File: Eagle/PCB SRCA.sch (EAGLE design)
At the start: 65 parts, among them IC1 DSPIC30F4011-30I_P, IC2 LM324LVIDR, IC3 LMT86QDCKRQ1, IC4 LORA_MOTE, J1 TBL002A-350-03GR-2OR, J2 TBL002A-350-03GR-2OR, J3 TBL002A-350-03GR-2OR, J4 172447-0004, J5 ICSP, Q1 TIP41C, T1 2N3904, T10 2N3904, T11 2N3904, T12 2N3904, T13 2N3904, T2 2N3904, T3 2N3904, T4 2N3904, T5 2N3904, T6 2N3904, T7 2N3904, T8 2N3904, T9 2N3904

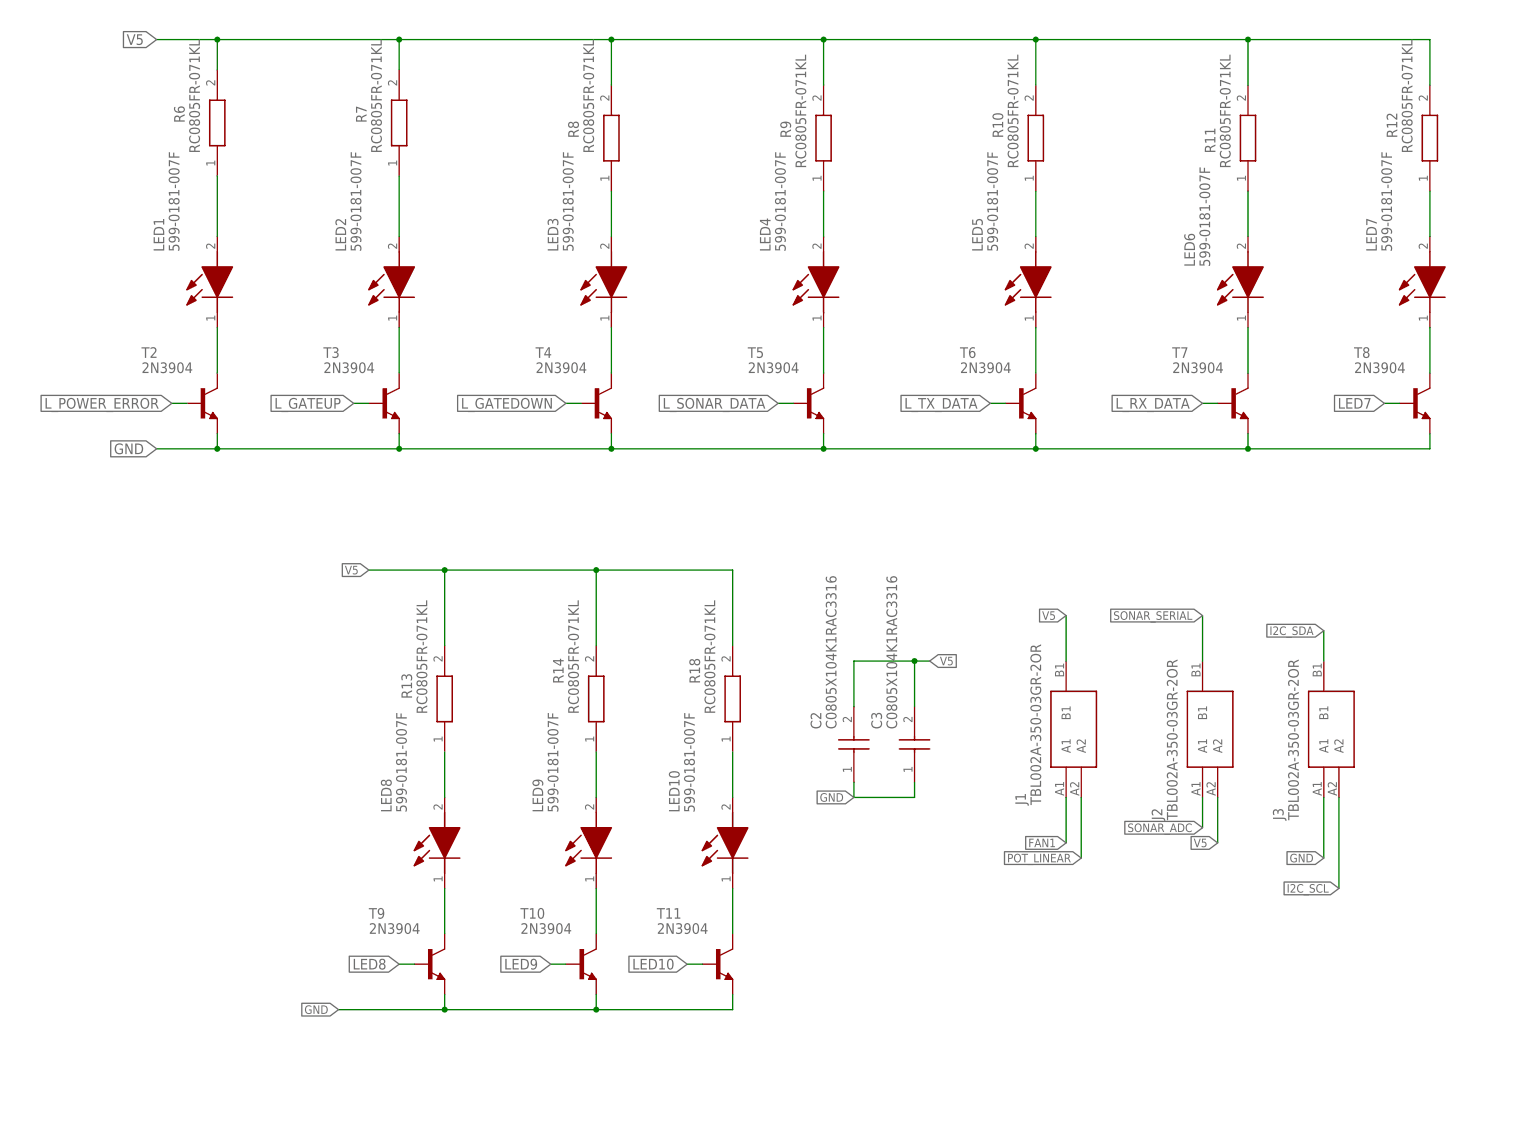
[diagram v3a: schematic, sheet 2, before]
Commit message: 11/08/2021
cambios pre finales del pcb y sus componentes
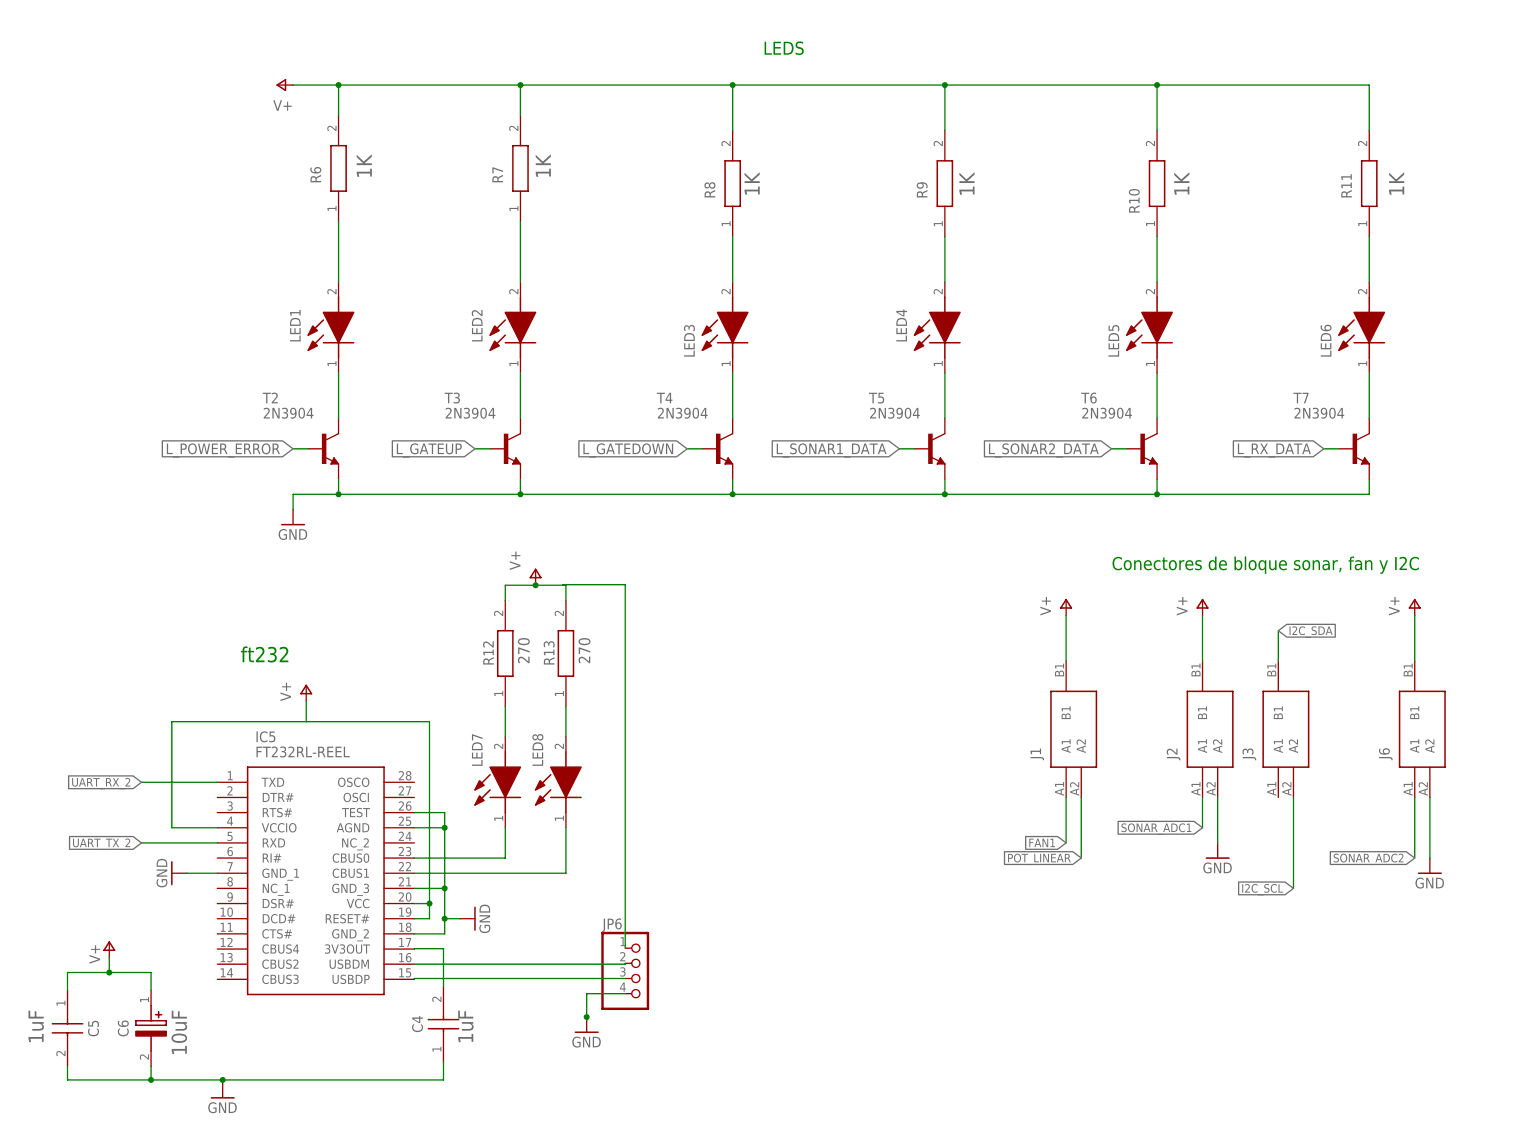
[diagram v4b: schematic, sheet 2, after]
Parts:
- removed LED10, LED9: 599-0181-007F, 599-0181-007F:599-0181-007F
- removed R14, R18: RC0805FR-071KL, RC0805FR-071KL:RC0805FR-071KL
- removed T10, T11, T8, T9: 2N3904, transistor-neu-to92:2N3904
- added C4, C5: C0805X104K1RAC3316, C0805X104K1RAC3316:C0805X104K1RAC3316
- added C6: UUP1C100MCL1GS, UUP1C100MCL1GS:UUP1C100MCL1GS
- added IC5: FT232RL-REEL, FT232RL-REEL:FT232RL-REEL
- added J6: TBL002A-350-03GR-2OR, TBL002A-350-03GR-2OR:TBL002A-350-03GR-2OR
- added J7: 44914-0401, 44914-0401:44914-0401
- added JP1, JP2, JP3, JP4: (no value), jumper:JP1E
- added JP5: (no value), pinhead:PINHD-1X6
- added JP6: (no value), pinhead:PINHD-1X4
- added ON: 599-0181-007F, 599-0181-007F:599-0181-007F
- added R24: RC0805FR-071KL, RC0805FR-071KL:RC0805FR-071KL
- added R25, R26: (no value), rcl:R-EU_0204/7
- added R27, R28: (no value), rcl:R-EU_0207/10
- C2, C3: value C0805X104K1RAC3316 -> TAJR104K020RNJ; device C0805X104K1RAC3316:C0805X104K1RAC3316 -> TAJR104K020RNJ:TAJR104K020RNJ
- J4: value 172447-0004 -> 44914-0801; device 172447-0004:172447-0004 -> 44914-0801:44914-0801
- R1: value RC0805FR-071KL -> (none); device RC0805FR-071KL:RC0805FR-071KL -> rcl:R-EU_0204/7
- renumbered LS1 to ICS
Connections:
- net N$3 renamed TEMP3
- net SONAR_ADC renamed SONAR_ADC1
- removed net LED10: IC1.OC4/RD3, T11.B
- removed net LED7: IC1.OSC2/CLKO/RC15, T8.B
- removed net LED8: IC1.!FLTA!/INT0/RE8, T9.B
- removed net LED9: IC1.EMUD2/OC2/IC2/INT2/RD1, T10.B
- removed net L_SONAR_DATA: IC1.AN6/OCFA/RB6, T5.B
- removed net L_TX_DATA: IC1.AN7/RB7, T6.B
- removed net N$13 (its old number): LED7.K, T8.C
- removed net SONAR_SERIAL: IC1.U2RX/CN17/RF4, J2.B1
- removed net TX_UART2: IC1.U2TX/CN18/RF5
- removed net V5: C2.2, C3.2, D1.C, IC1.VDD_1, IC1.VDD_3, IC2.V+, IC3.VDD_1, IC4.V5, ICS.1, J1.B1, J2.A2, J4.4, J5.VDD, R1.2, R10.2, R11.2, R12.2, R13.2, R14.2, R17.2, R18.2, R19.2, R2.2, R6.2, R7.2, R8.2, R9.2, S2.NO_1, S3.NO_2, S4.NO_1
- new net BIT_1: IC1.PWM2L/RE2, J4.1
- new net BIT_2: IC1.PWM2H/RE3, J4.2
- new net BIT_3: IC1.PWM3L/RE4, J4.3
- new net BIT_4: IC1.PWM3H/RE5, J4.4
- new net BIT_5: IC1.C1RX/RF0, J4.5
- new net BIT_6: IC1.C1TX/RF1, J4.6
- new net BIT_7: IC1.SCK1/RF6, J4.7
- new net BIT_8: IC1.EMUC2/OC1/IC1/INT1/RD0, J4.8
- new net L_SONAR1_DATA: IC1.AN8/RB8, T5.B
- new net L_SONAR2_DATA: IC1.OSC2/CLKO/RC15, T6.B
- new net N$18: IC5.CBUS1, LED8.K
- new net N$19: JP6.1
- new net N$27: IC2.IN4+, R27.1, R28.2
- new net N$28: ON.A, R24.1
- new net N$29: JP2.1, R22.2
- new net N$30: JP1.1, R19.1, T13.C
- new net POWER: IC1.AN2/!SS1!/CN4/RB2, IC2.IN4-, IC2.OUT4
- new net SONAR_ADC2: IC1.EMUC3/AN1/VREF-/CN3/RB1, J6.A1
- new net TEMP1: JP4.1, R25.1
- new net TEMP2: JP3.2, R26.1
- new net UART_RX_2: IC1.U2RX/CN17/RF4, IC5.TXD
- new net UART_TX_2: IC1.U2TX/CN18/RF5, IC5.RXD
- new net V+: C2.+, C3.+, C5.1, C6.+, D1.C, IC1.VDD_1, IC1.VDD_3, IC2.V+, IC3.VDD_1, IC4.V5, ICS.1, J1.B1, J2.B1, J5.VDD, J6.B1, J7.2, J7.4, JP5.5, R1.2, R10.2, R11.2, R12.2, R13.2, R17.2, R19.2, R2.2, R24.2, R25.2, R26.2, R27.2, R6.2, R7.2, R8.2, R9.2, S2.NO_1, S3.NO_1
- net AVAILABLE: now also R5.2, S2.COM_2; no longer R3.2, S4.COM_1
- net GATE_DOWN: now also IC1.OC4/RD3; no longer IC1.EMUC2/OC1/IC1/INT1/RD0
- net GATE_UP: now also IC1.EMUD2/OC2/IC2/INT2/RD1, R3.2, S4.COM_2; no longer IC1.SCK1/RF6, R5.2, S2.COM_1
- net GND: now also C2.-, C3.-, C4.1, C5.2, C6.-, IC5.AGND, IC5.GND_1, IC5.GND_2, IC5.GND_3, IC5.TEST, J2.A2, J6.A2, J7.1, J7.3, JP5.6, JP6.4, ON.K, R28.1; no longer C2.1, C3.1, J3.A1, J4.3, T10.E, T11.E, T8.E, T9.E
- net I2C_SCL: now also JP4.2, JP5.3
- net I2C_SDA: now also JP3.1, JP5.4
- net L_GATEDOWN: now also IC1.AN7/RB7; no longer IC1.AN5/QEB/IC8/CN7/RB5
- net L_GATEUP: now also IC1.AN6/OCFA/RB6; no longer IC1.AN4/QEA/IC7/CN6/RB4
- net L_POWER_ERROR: now also IC1.AN5/QEB/IC8/CN7/RB5; no longer IC1.AN3/INDX/CN5/RB3
- net L_RX_DATA: now also IC1.!FLTA!/INT0/RE8; no longer IC1.AN8/RB8
- net MCLR: now also S1.NO_1; no longer S1.NO_2
- net N$1: now also S3.NO_2, S4.NO_1; no longer LED10.K, T11.C
- net N$14: now also IC5.RESET#, IC5.VCC, IC5.VCCIO; no longer LED8.K, T9.C
- net N$15: now also IC5.CBUS0, LED7.K; no longer LED9.K, T10.C
- net N$20: now also C4.2, IC5.3V3OUT; no longer S3.NO_1
- net N$21: now also IC5.USBDM, JP6.2; no longer LED9.A, R14.1
- net N$22: now also IC5.USBDP, JP6.3; no longer LED10.A, R18.1
- net POT_LINEAR: now also IC1.AN4/QEA/IC7/CN6/RB4; no longer IC1.AN2/!SS1!/CN4/RB2
- net RX_UART: now also JP1.2; no longer R19.1, T13.C
- net TEMP: now also IC1.AN3/INDX/CN5/RB3; no longer IC1.EMUC3/AN1/VREF-/CN3/RB1
- net TX_UART: now also JP2.2; no longer R22.2
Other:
- note added: "10uF"
- note added: "1K"
- note added: "1uF"
- note added: "270"
- note added: "Amplificador de temp y seguidor de voltaje"
- note added: "Conector de alimentacion"
- note added: "Conectores de bloque sonar, fan y I2C"
- note added: "DSPIC"
- note added: "LEDS"
- note added: "RTC"
- note added: "cap Dspic"
- note added: "conector de 8bits"
- note added: "ft232"
- note added: "puerto de pickit"
- note added: "pulsadores"
- note added: "resistencia pull up I2C"
- moved on the sheet: C1, IC2, IC3, J3, J5, LED1, LED2, LED3, LED4, LED5, LED6, LED7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

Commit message: 12/08/2021
correccion de sensor de temperatura
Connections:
- net GND: now also IC3.GND_2
- net V+: now also IC3.VDD_2
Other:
- note added: "10k"
- note added: "1k"
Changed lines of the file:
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@@
 <setting verticaltext="up"/>
 </settings>
-<grid distance="1" unitdist="mm" unit="mm" style="lines" multiple="1" display="no" altdistance="1" altunitdist="mm" altunit="mm"/>
+<grid distance="0.1" unitdist="inch" unit="inch" style="lines" multiple="1" display="no" altdistance="0.01" altunitdist="inch" altunit="inch"/>
 <layers>
 <layer number="1" name="Top" color="4" fill="1" visible="no" active="no"/>
@@
 <text x="190.5" y="81.28" size="2.1844" layer="91">RTC</text>
 <text x="68.58" y="180.34" size="2.1844" layer="91">DSPIC</text>
+<text x="194" y="154" size="1.9304" layer="96" rot="R90">1k</text>
+<text x="13" y="32" size="1.9304" layer="96" rot="R90">1k</text>
+<text x="54" y="30" size="1.9304" layer="96" rot="R90">1k</text>
+<text x="61" y="78" size="1.9304" layer="96" rot="R90">1k</text>
+<text x="37" y="95" size="1.9304" layer="96" rot="R90">10k</text>
+<text x="160" y="45" size="1.9304" layer="96">1k</text>
+<text x="157" y="59" size="1.9304" layer="96" rot="R90">1k</text>
 </plain>
 <instances>
@@
 <pinref part="GND18" gate="1" pin="GND"/>
 <pinref part="IC3" gate="G$1" pin="GND_1"/>
+<pinref part="IC3" gate="G$1" pin="GND_2"/>
+<wire x1="101.6" y1="25.4" x2="99.06" y2="25.4" width="0.1524" layer="91"/>
+<wire x1="99.06" y1="25.4" x2="99.06" y2="27.94" width="0.1524" layer="91"/>
+<junction x="99.06" y="27.94"/>
 </segment>
 <segment>
@@
 </segment>
 <segment>
-<wire x1="132.08" y1="27.94" x2="134.62" y2="27.94" width="0.1524" layer="91"/>
-<pinref part="P+14" gate="1" pin="V+"/>
-<pinref part="IC3" gate="G$1" pin="VDD_1"/>
-</segment>
-<segment>
 <pinref part="P+19" gate="1" pin="V+"/>
 <pinref part="R27" gate="G$1" pin="2"/>
@@
 <pinref part="P+5" gate="1" pin="V+"/>
 </segment>
-</net>
+<segment>
+<pinref part="P+14" gate="1" pin="V+"/>
+<pinref part="IC3" gate="G$1" pin="VDD_1"/>
+<wire x1="134.62" y1="27.94" x2="132.08" y2="27.94" width="0.1524" layer="91"/>
+<pinref part="IC3" gate="G$1" pin="VDD_2"/>
+<wire x1="132.08" y1="25.4" x2="134.62" y2="25.4" width="0.1524" layer="91"/>
+<wire x1="134.62" y1="25.4" x2="134.62" y2="27.94" width="0.1524" layer="91"/>
+<junction x="134.62" y="27.94"/>
+</segment>
+</net>

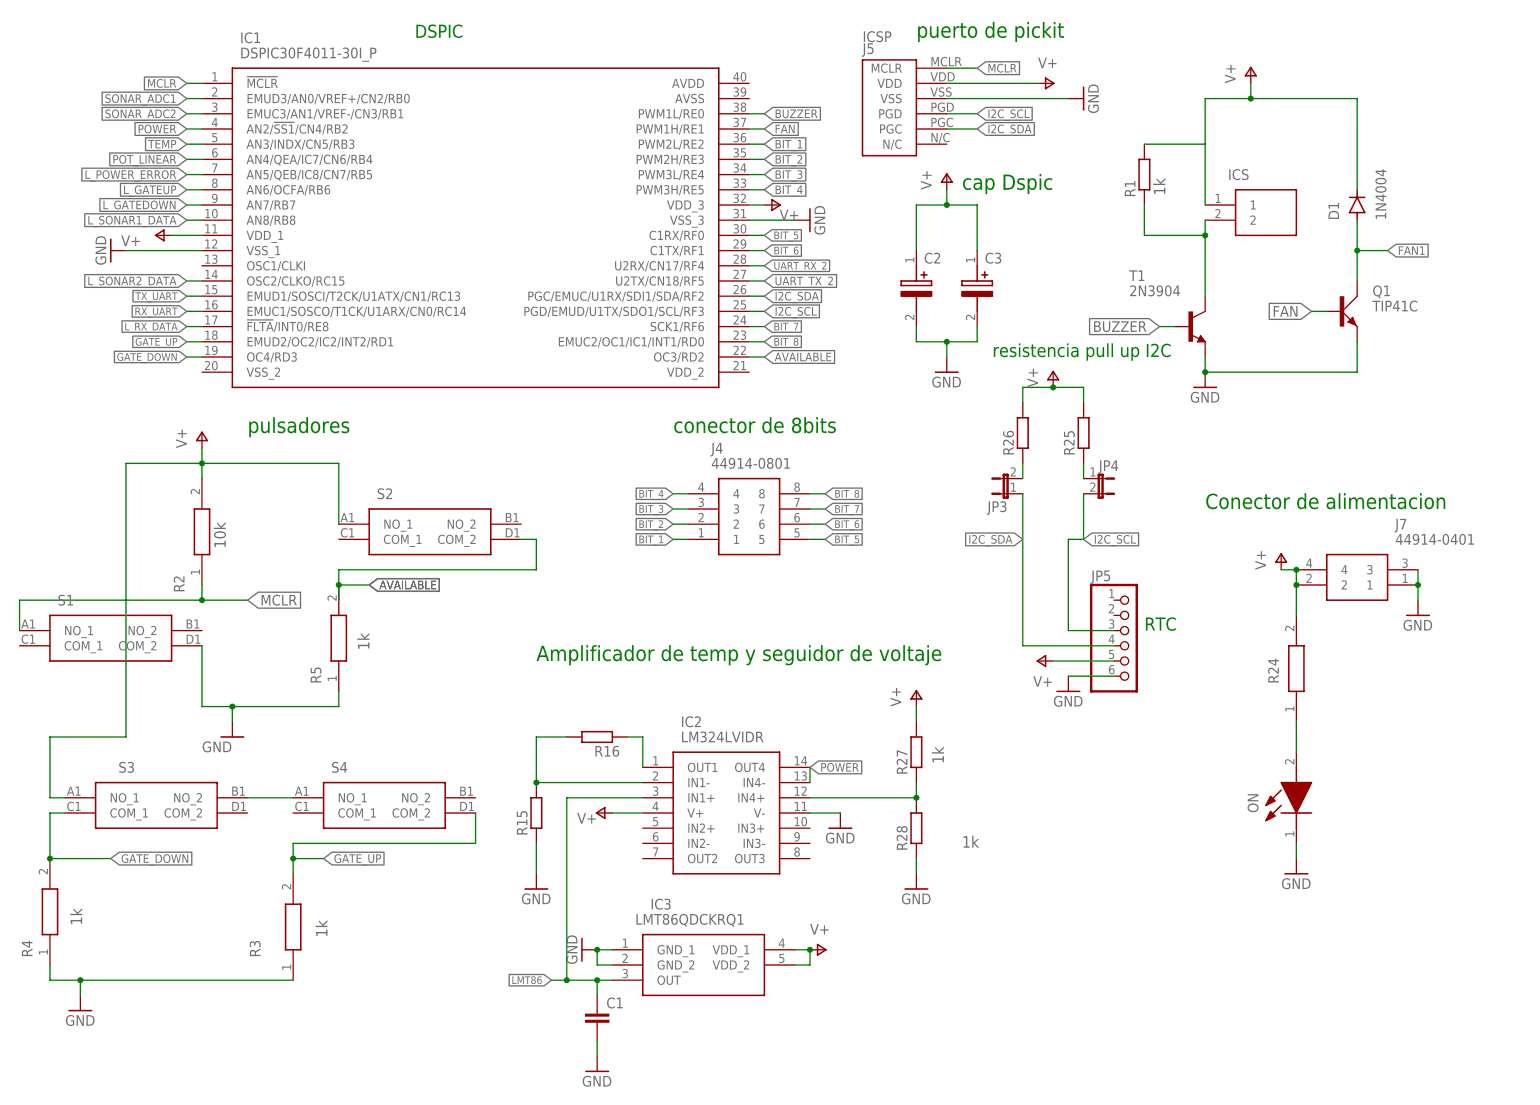
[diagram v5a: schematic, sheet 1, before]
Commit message: 20/08/2021
se adjunta los archivos de la PCB  final con logo  y archivo gerber
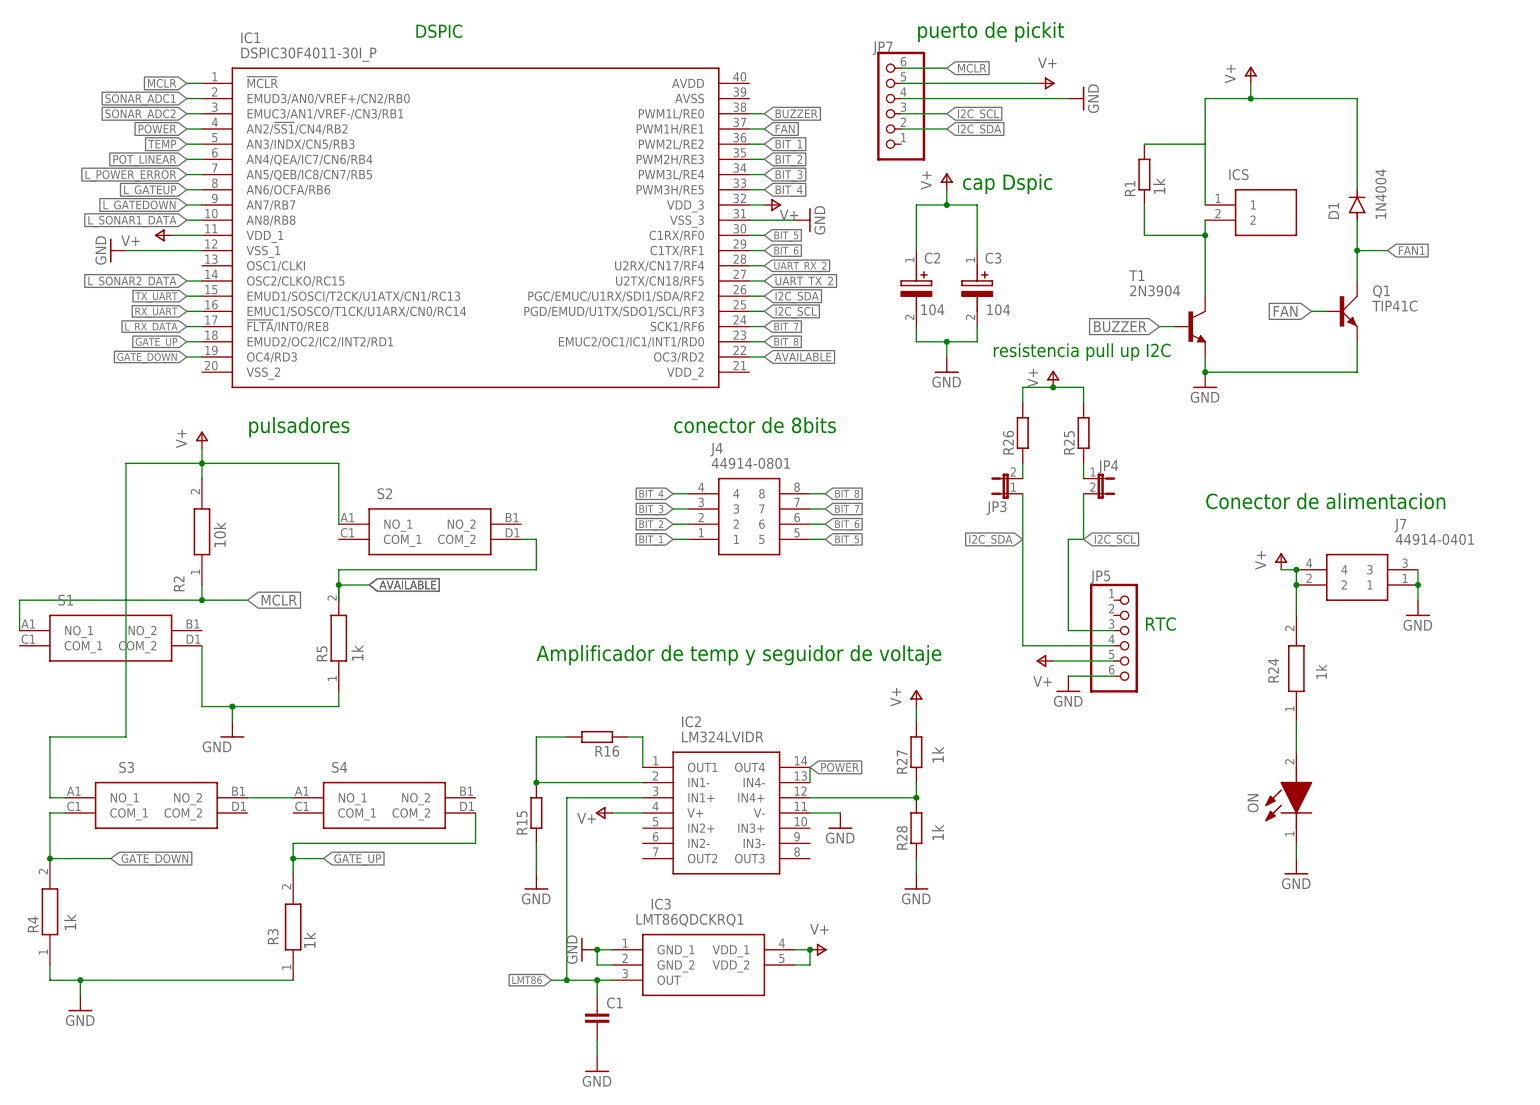
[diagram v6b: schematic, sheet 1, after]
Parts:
- removed J5: ICSP, ICSP:ICSP
- added JP7: (no value), pinhead:PINHD-1X6
- renumbered IC4 to ICS1
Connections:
- removed net N$19: JP6.1
- net GND: now also JP7.4; no longer J5.VSS
- net I2C_SCL: now also JP7.3; no longer J5.PGD
- net I2C_SDA: now also JP7.2; no longer J5.PGC
- net MCLR: now also JP7.6; no longer J5.MCLR
- net V+: now also JP6.1, JP7.5; no longer J5.VDD
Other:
- note added: "104"
- note added: "5.1k"
- note added: "transductor de voltaje 3.3 to 5V"
- note added: "transductor de voltaje 5 to 3.3V"
